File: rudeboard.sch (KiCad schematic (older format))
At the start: 131 parts, among them U1 Elite-C

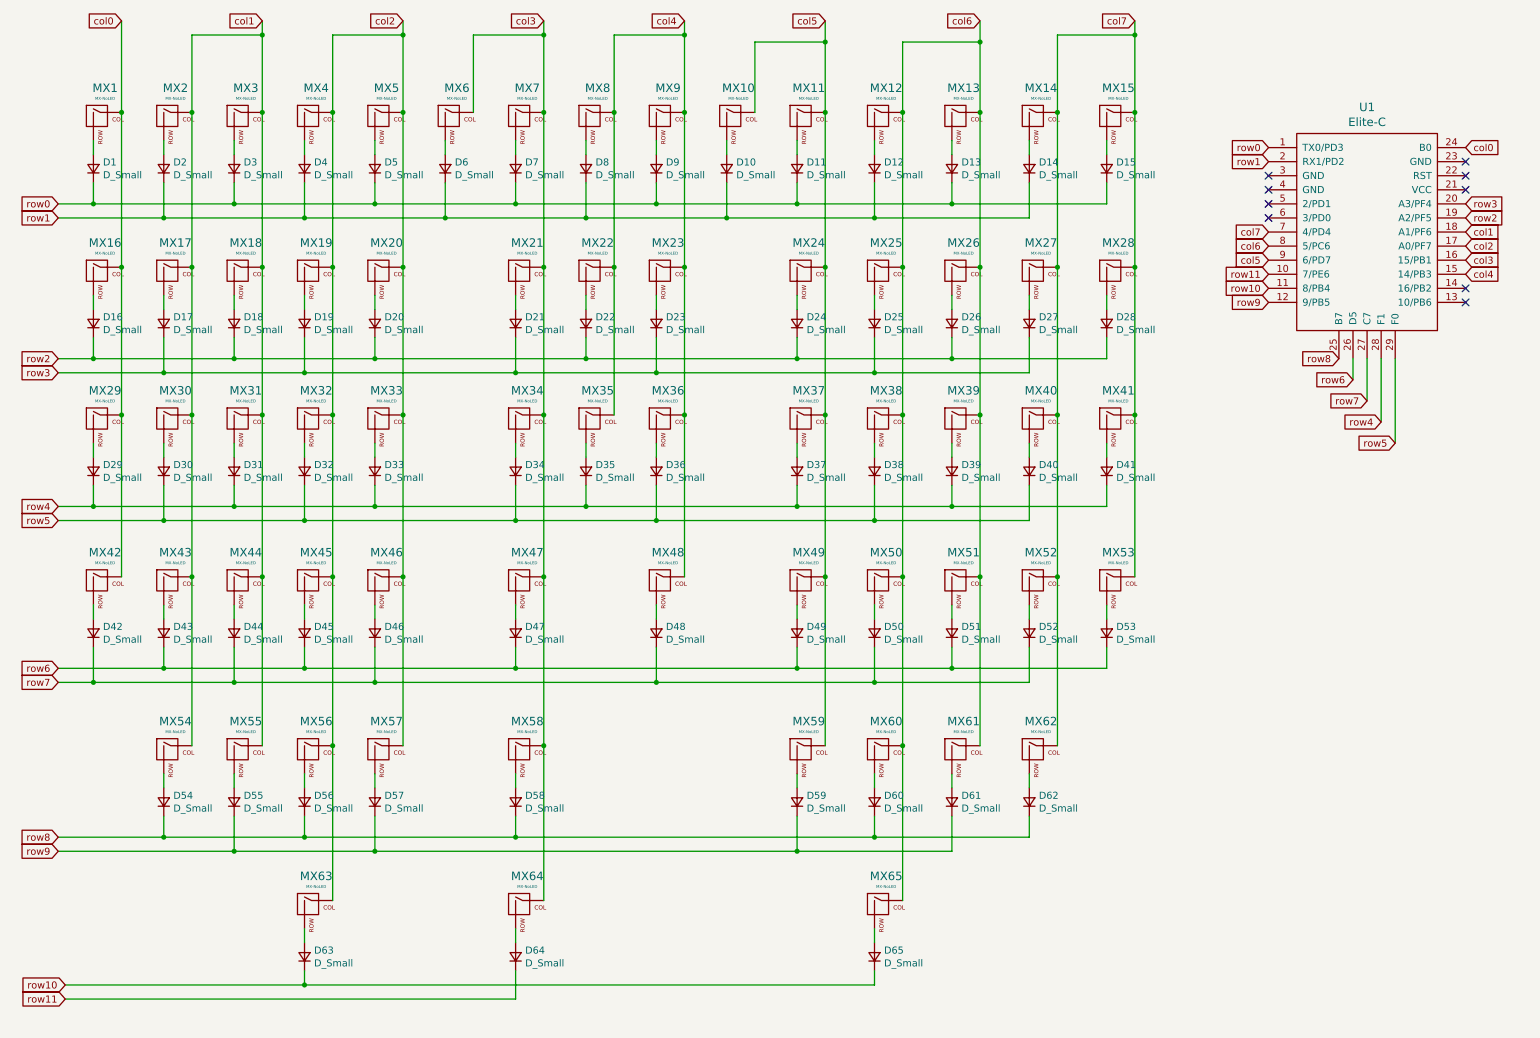
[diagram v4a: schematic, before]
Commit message: v1.2
- using traditional matrix -- duplex matrix didn't provide any benifit
- still dependant on elite-c
- much better looking pcb
- everything else is same
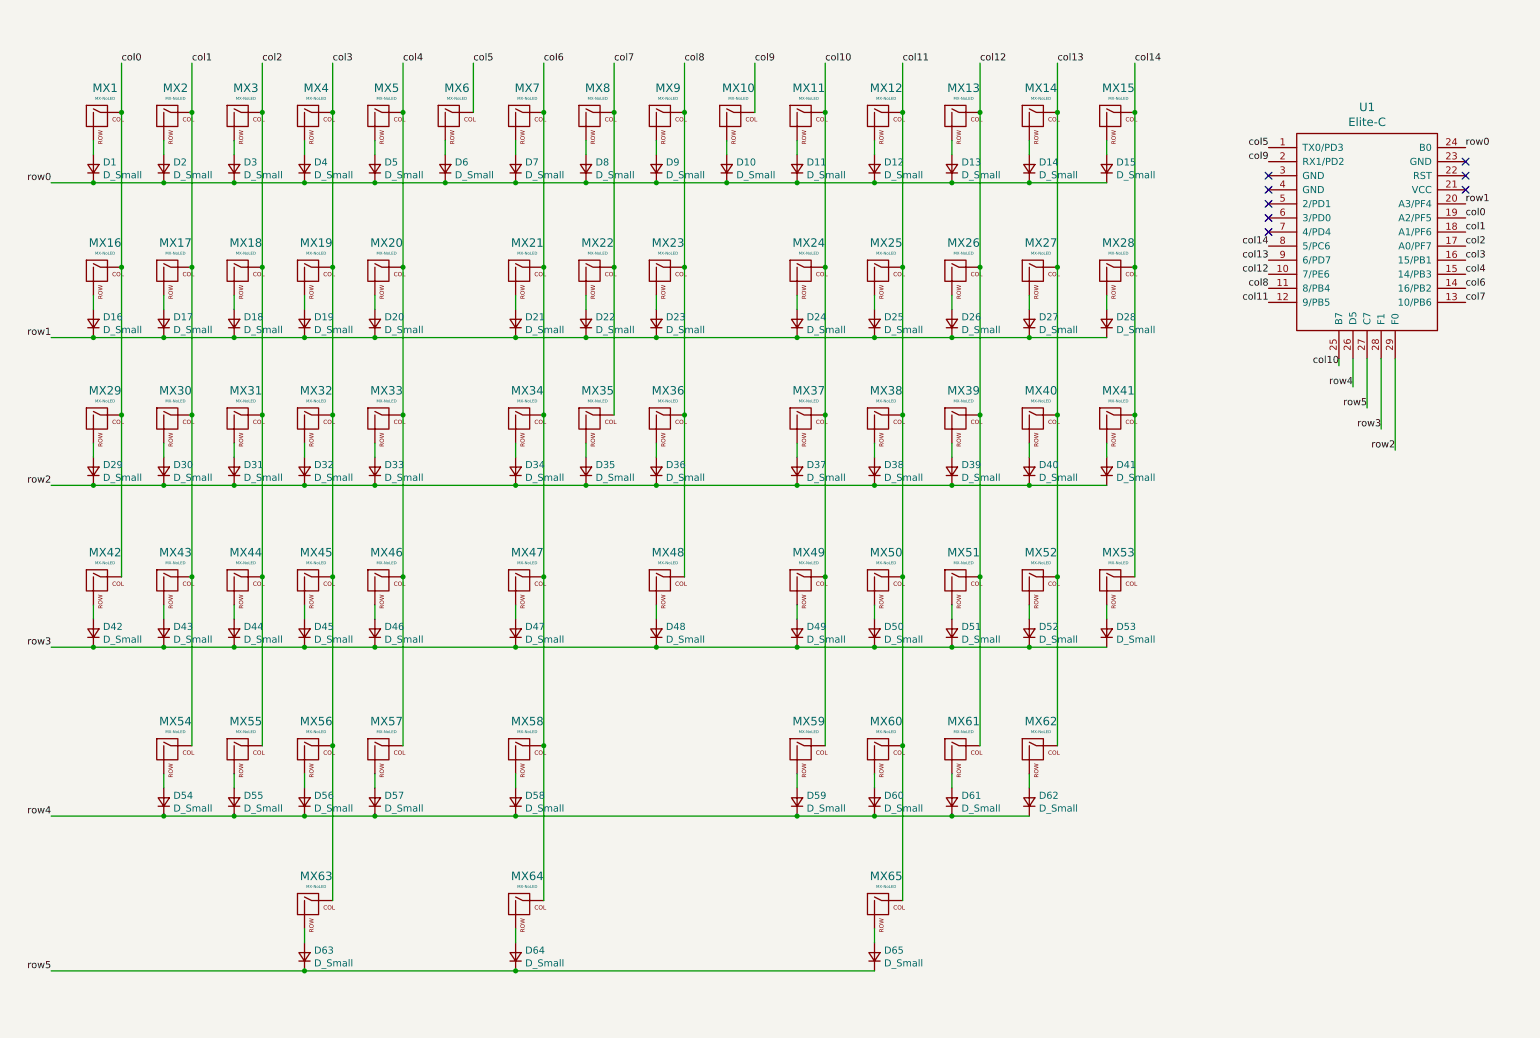
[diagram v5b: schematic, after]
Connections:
- net col0: now also U1.19 (A2/PF5); no longer U1.24 (B0)
- net col1: no longer MX18.1 (COL), MX3.1 (COL), MX31.1 (COL), MX44.1 (COL), MX55.1 (COL)
- net col2: now also MX18.1 (COL), MX3.1 (COL), MX31.1 (COL), MX44.1 (COL), MX55.1 (COL); no longer MX19.1 (COL), MX20.1 (COL), MX32.1 (COL), MX33.1 (COL), MX4.1 (COL), MX45.1 (COL), MX46.1 (COL), MX5.1 (COL), MX56.1 (COL), MX57.1 (COL), MX63.1 (COL)
- net col3: now also MX19.1 (COL), MX32.1 (COL), MX4.1 (COL), MX45.1 (COL), MX56.1 (COL), MX63.1 (COL); no longer MX21.1 (COL), MX34.1 (COL), MX47.1 (COL), MX58.1 (COL), MX6.1 (COL), MX64.1 (COL), MX7.1 (COL)
- net col4: now also MX20.1 (COL), MX33.1 (COL), MX46.1 (COL), MX5.1 (COL), MX57.1 (COL); no longer MX22.1 (COL), MX23.1 (COL), MX35.1 (COL), MX36.1 (COL), MX48.1 (COL), MX8.1 (COL), MX9.1 (COL)
- net col5: now also MX6.1 (COL), U1.1 (TX0/PD3); no longer MX10.1 (COL), MX11.1 (COL), MX24.1 (COL), MX37.1 (COL), MX49.1 (COL), MX59.1 (COL), U1.9 (6/PD7)
- net col6: now also MX21.1 (COL), MX34.1 (COL), MX47.1 (COL), MX58.1 (COL), MX64.1 (COL), MX7.1 (COL), U1.14 (16/PB2); no longer MX12.1 (COL), MX13.1 (COL), MX25.1 (COL), MX26.1 (COL), MX38.1 (COL), MX39.1 (COL), MX50.1 (COL), MX51.1 (COL), MX60.1 (COL), MX61.1 (COL), MX65.1 (COL), U1.8 (5/PC6)
- net col7: now also MX22.1 (COL), MX35.1 (COL), MX8.1 (COL), U1.13 (10/PB6); no longer MX14.1 (COL), MX15.1 (COL), MX27.1 (COL), MX28.1 (COL), MX40.1 (COL), MX41.1 (COL), MX52.1 (COL), MX53.1 (COL), MX62.1 (COL), U1.7 (4/PD4)
- net row0: now also D10.1 (K), D12.1 (K), D14.1 (K), D2.1 (K), D4.1 (K), D6.1 (K), D8.1 (K), U1.24 (B0); no longer U1.1 (TX0/PD3)
- net row1: now also D16.1 (K), D17.1 (K), D18.1 (K), D19.1 (K), D20.1 (K), D21.1 (K), D22.1 (K), D23.1 (K), D24.1 (K), D25.1 (K), D26.1 (K), D27.1 (K), D28.1 (K), U1.20 (A3/PF4); no longer D10.1 (K), D12.1 (K), D14.1 (K), D2.1 (K), D4.1 (K), D6.1 (K), D8.1 (K), U1.2 (RX1/PD2)
- net row2: now also D29.1 (K), D30.1 (K), D31.1 (K), D32.1 (K), D33.1 (K), D34.1 (K), D35.1 (K), D36.1 (K), D37.1 (K), D38.1 (K), D39.1 (K), D40.1 (K), D41.1 (K), U1.29 (F0); no longer D16.1 (K), D18.1 (K), D20.1 (K), D22.1 (K), D24.1 (K), D26.1 (K), D28.1 (K), U1.19 (A2/PF5)
- net row3: now also D42.1 (K), D43.1 (K), D44.1 (K), D45.1 (K), D46.1 (K), D47.1 (K), D48.1 (K), D49.1 (K), D50.1 (K), D51.1 (K), D52.1 (K), D53.1 (K), U1.28 (F1); no longer D17.1 (K), D19.1 (K), D21.1 (K), D23.1 (K), D25.1 (K), D27.1 (K), U1.20 (A3/PF4)
- net row4: now also D54.1 (K), D55.1 (K), D56.1 (K), D57.1 (K), D58.1 (K), D59.1 (K), D60.1 (K), D61.1 (K), D62.1 (K), U1.26 (D5); no longer D29.1 (K), D31.1 (K), D33.1 (K), D35.1 (K), D37.1 (K), D39.1 (K), D41.1 (K), U1.28 (F1)
- net row5: now also D63.1 (K), D64.1 (K), D65.1 (K), U1.27 (C7); no longer D30.1 (K), D32.1 (K), D34.1 (K), D36.1 (K), D38.1 (K), D40.1 (K), U1.29 (F0)
- removed net row10: D63.1 (K), D65.1 (K), U1.11 (8/PB4)
- net row11 renamed col12
- net col12: now also MX13.1 (COL), MX26.1 (COL), MX39.1 (COL), MX51.1 (COL), MX61.1 (COL); no longer D64.1 (K)
- removed net row6: D43.1 (K), D45.1 (K), D47.1 (K), D49.1 (K), D51.1 (K), D53.1 (K), U1.26 (D5)
- removed net row7: D42.1 (K), D44.1 (K), D46.1 (K), D48.1 (K), D50.1 (K), D52.1 (K), U1.27 (C7)
- removed net row8: D54.1 (K), D56.1 (K), D58.1 (K), D60.1 (K), D62.1 (K), U1.25 (B7)
- removed net row9: D55.1 (K), D57.1 (K), D59.1 (K), D61.1 (K), U1.12 (9/PB5)
- new net col10: MX11.1 (COL), MX24.1 (COL), MX37.1 (COL), MX49.1 (COL), MX59.1 (COL), U1.25 (B7)
- new net col11: MX12.1 (COL), MX25.1 (COL), MX38.1 (COL), MX50.1 (COL), MX60.1 (COL), MX65.1 (COL), U1.12 (9/PB5)
- new net col13: MX14.1 (COL), MX27.1 (COL), MX40.1 (COL), MX52.1 (COL), MX62.1 (COL), U1.9 (6/PD7)
- new net col14: MX15.1 (COL), MX28.1 (COL), MX41.1 (COL), MX53.1 (COL), U1.8 (5/PC6)
- new net col8: MX23.1 (COL), MX36.1 (COL), MX48.1 (COL), MX9.1 (COL), U1.11 (8/PB4)
- new net col9: MX10.1 (COL), U1.2 (RX1/PD2)
- no-connect marks 9 -> 8

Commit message: update schamatic to integrate mcu
- use atmega32u4 as mcu
- complete schamatics
- row/cols not final
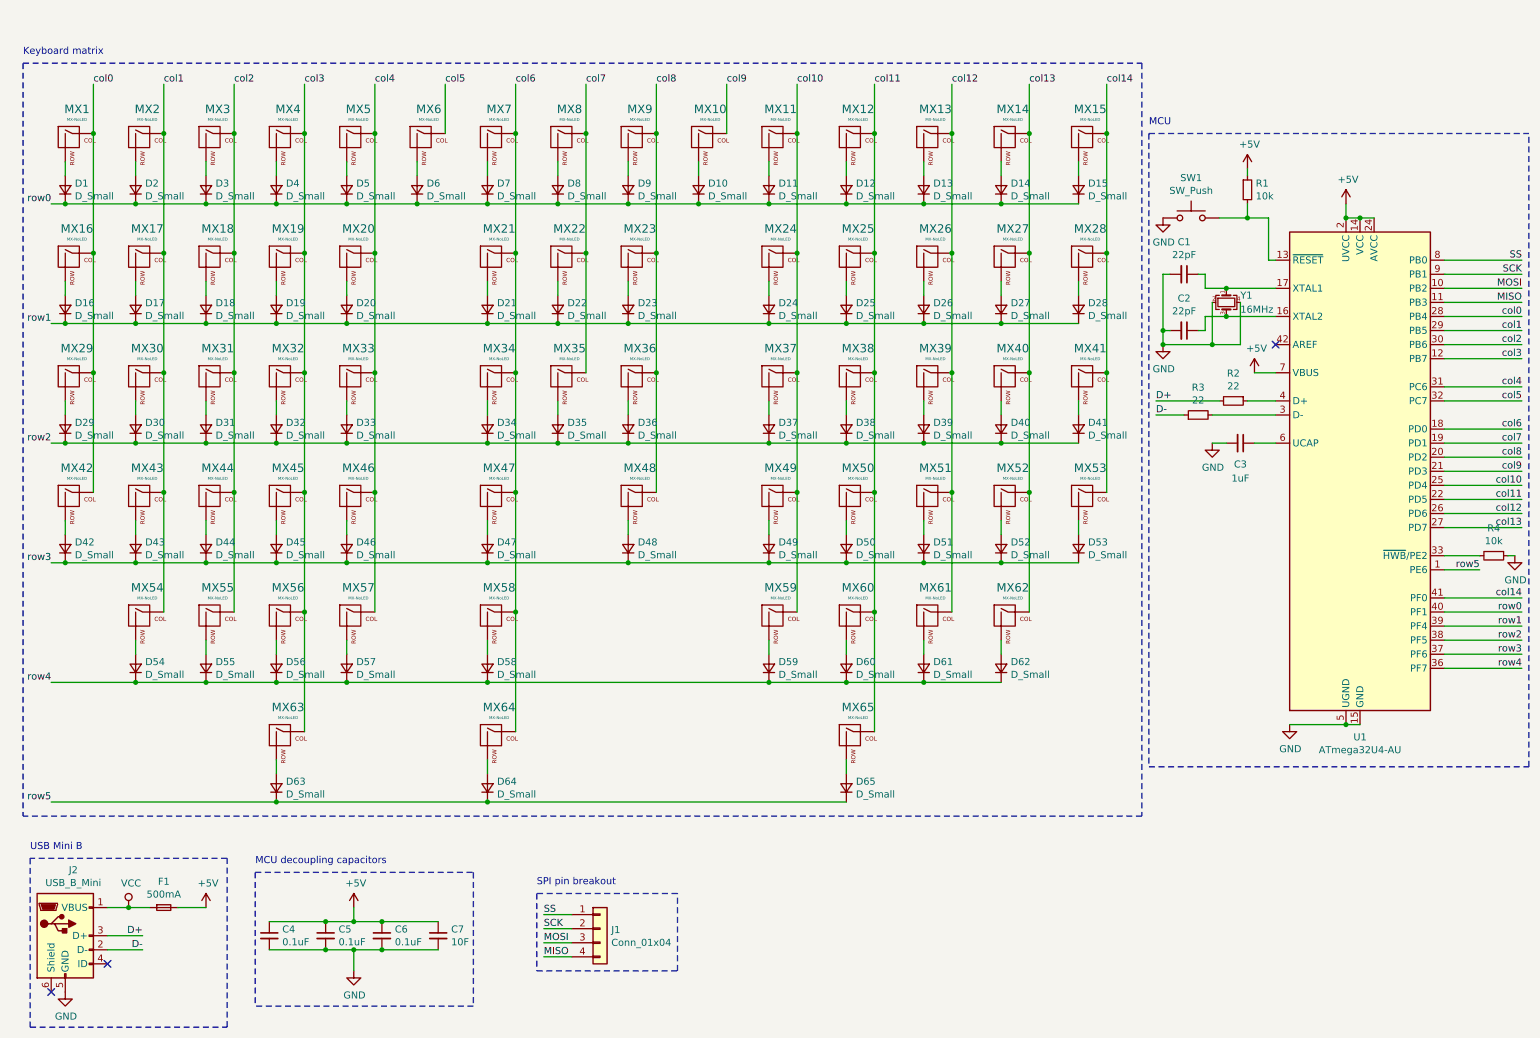
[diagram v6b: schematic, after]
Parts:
- removed U1: Elite-C, Keebio_Parts:Elite-C, symbol keebio:Elite-C
- added C1, C2: 22pF, Capacitor_SMD:C_0805_2012Metric_Pad1.15x1.40mm_HandSolder, symbol Device:C_Small
- added C3: 1uF, Capacitor_SMD:C_0805_2012Metric_Pad1.15x1.40mm_HandSolder, symbol Device:C_Small
- added C4, C5, C6: 0.1uF, Capacitor_SMD:C_0805_2012Metric_Pad1.15x1.40mm_HandSolder, symbol Device:C_Small
- added C7: 10F, Capacitor_SMD:C_0805_2012Metric_Pad1.15x1.40mm_HandSolder, symbol Device:C_Small
- added F1: 500mA, Fuse:Fuse_1206_3216Metric_Pad1.42x1.75mm_HandSolder, symbol Device:Fuse_Small
- added J1: Conn_01x04, Connector_PinHeader_2.54mm:PinHeader_1x04_P2.54mm_Vertical, symbol Connector_Generic:Conn_01x04
- added J2: USB_B_Mini, Keebio-Parts:USB-Mini-B_ LCSC-C46398, symbol Connector:USB_B_Mini
- added R1, R4: 10k, Resistor_SMD:R_0805_2012Metric_Pad1.15x1.40mm_HandSolder, symbol Device:R_Small
- added R2, R3: 22, Resistor_SMD:R_0805_2012Metric_Pad1.15x1.40mm_HandSolder, symbol Device:R_Small
- added SW1: SW_Push, Button_Switch_SMD:SW_SPST_SKQG_WithStem, symbol Switch:SW_Push
- added U1: ATmega32U4-AU, Package_QFP:TQFP-44_10x10mm_P0.8mm, symbol MCU_Microchip_ATmega:ATmega32U4-AU
- added Y1: 16MHz, Crystal:Crystal_SMD_3225-4Pin_3.2x2.5mm, symbol Device:Crystal_GND24_Small
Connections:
- net col0: now also U1.28 (PB4)
- net col1: now also U1.29 (PB5)
- net col10: now also U1.25 (PD4)
- net col11: now also U1.22 (PD5)
- net col12: now also U1.26 (PD6)
- net col13: now also U1.27 (PD7)
- net col14: now also U1.41 (PF0)
- net col2: now also U1.30 (PB6)
- net col3: now also U1.12 (PB7)
- net col4: now also U1.31 (PC6)
- net col5: now also U1.32 (PC7)
- net col6: now also U1.18 (PD0)
- net col7: now also U1.19 (PD1)
- net col8: now also U1.20 (PD2)
- net col9: now also U1.21 (PD3)
- net row0: now also U1.40 (PF1)
- net row1: now also U1.39 (PF4)
- net row2: now also U1.38 (PF5)
- net row3: now also U1.37 (PF6)
- net row4: now also U1.36 (PF7)
- net row5: now also U1.1 (PE6)
- new net: R1.2, SW1.2, U1.13 (~RESET)
- new net: C2.1, U1.16 (XTAL2), Y1.3
- new net: C1.1, U1.17 (XTAL1), Y1.1
- new net: R3.2, U1.3 (D-)
- new net: R4.2, U1.33 (~HWB~/PE2)
- new net: R2.1, U1.4 (D+)
- new net: C3.1, U1.6 (UCAP)
- new net +5V: C4.1, C5.1, C6.1, C7.1, F1.2, R1.1, U1.14 (VCC), U1.2 (UVCC), U1.24 (AVCC), U1.34 (VCC), U1.44 (AVCC), U1.7 (VBUS)
- new net D+: J2.3 (D+), R2.2
- new net D-: J2.2 (D-), R3.1
- new net GND: C1.2, C2.2, C3.2, C4.2, C5.2, C6.2, C7.2, J2.5 (GND), R4.1, SW1.1, U1.15 (GND), U1.23 (GND), U1.35 (GND), U1.43 (GND), U1.5 (UGND), Y1.2, Y1.4
- new net MISO: J1.4 (Pin_4), U1.11 (PB3)
- new net MOSI: J1.3 (Pin_3), U1.10 (PB2)
- new net SCK: J1.2 (Pin_2), U1.9 (PB1)
- new net SS: J1.1 (Pin_1), U1.8 (PB0)
- new net VCC: F1.1, J2.1 (VBUS)
- no-connect marks 8 -> 3
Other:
- note added: "Keyboard matrix"
- note added: "MCU"
- note added: "MCU decoupling capacitors"
- note added: "SPI pin breakout"
- note added: "USB Mini B"
- moved on the sheet: D1, D10, D11, D12, D13, D14, D15, D16, D17, D18, D19, D2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
